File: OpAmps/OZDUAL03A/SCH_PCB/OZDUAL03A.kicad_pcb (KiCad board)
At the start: 2 copper layers, 40.4 x 40.4 mm, 53 parts, among them Con1 47u, Con2 47u, Con3 47u, Con4 47u, J1 JUMP2_2x1, J2 POWER, J3 OPAMPA, J4 OPAMPB, J5 SOT23-6, M1 HOLE, M2 HOLE, M3 HOLE, M4 HOLE, U1 OZ, U2 sot23-6

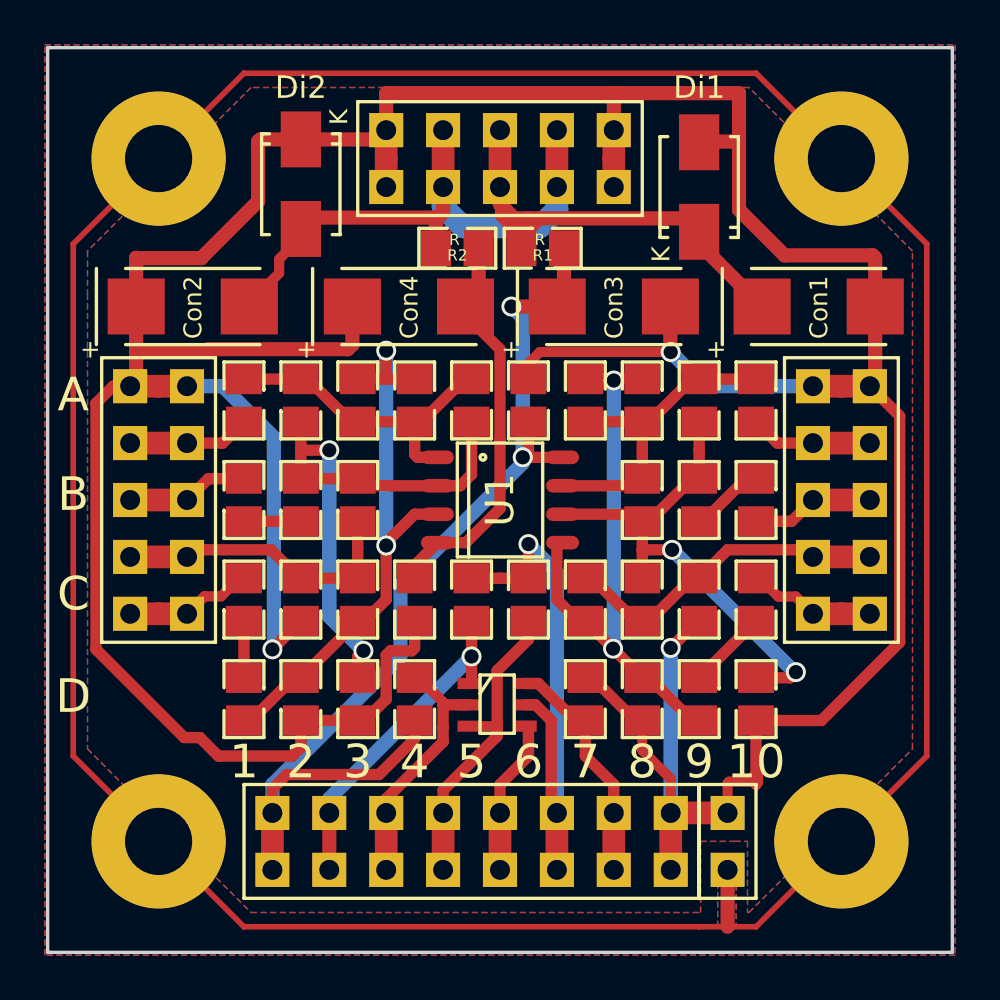
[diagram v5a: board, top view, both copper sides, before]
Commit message: uprava prokovu, zvetseni mezery pod soucastkama
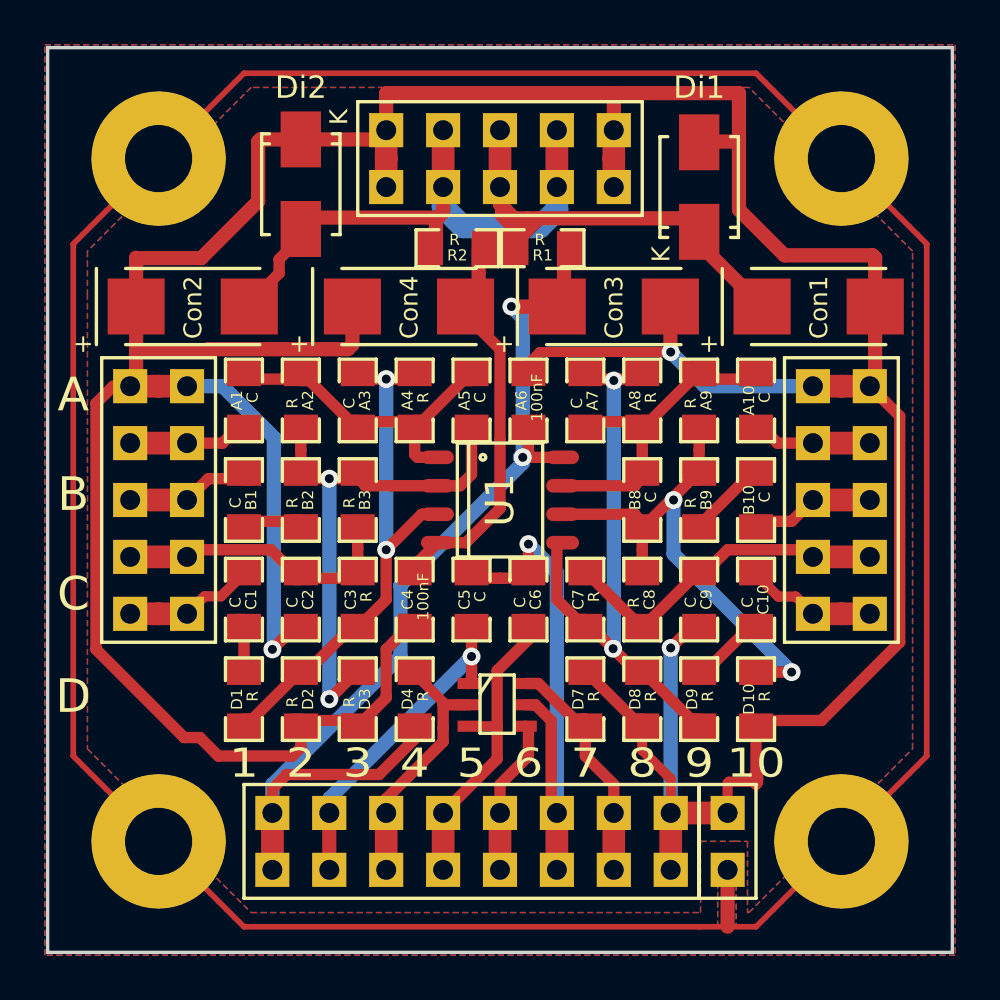
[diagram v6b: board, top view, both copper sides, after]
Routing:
- net Net-(A3-Pad1): track 26.9 -> 24.2 mm
- net Net-(A9-Pad2): track 23.4 -> 24.4 mm
